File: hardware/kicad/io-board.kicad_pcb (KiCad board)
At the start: 2 copper layers, 160 x 75 mm, 54 parts, among them J1 NCJ6FI-S, J2 NCJ6FI-S, J3 NCJ6FI-S, J4 NCJ6FI-S, P1 JIO-PWR, P2 JIO-WETSEND, P3 JIO-WETRET, P4 JIO-DRY, P5 Wet/Dry control, P6 Mono switch, U1 OPA1644AIDR, U2 OPA1656IDR, U3 OPA1656IDR, U4 OPA1656IDR

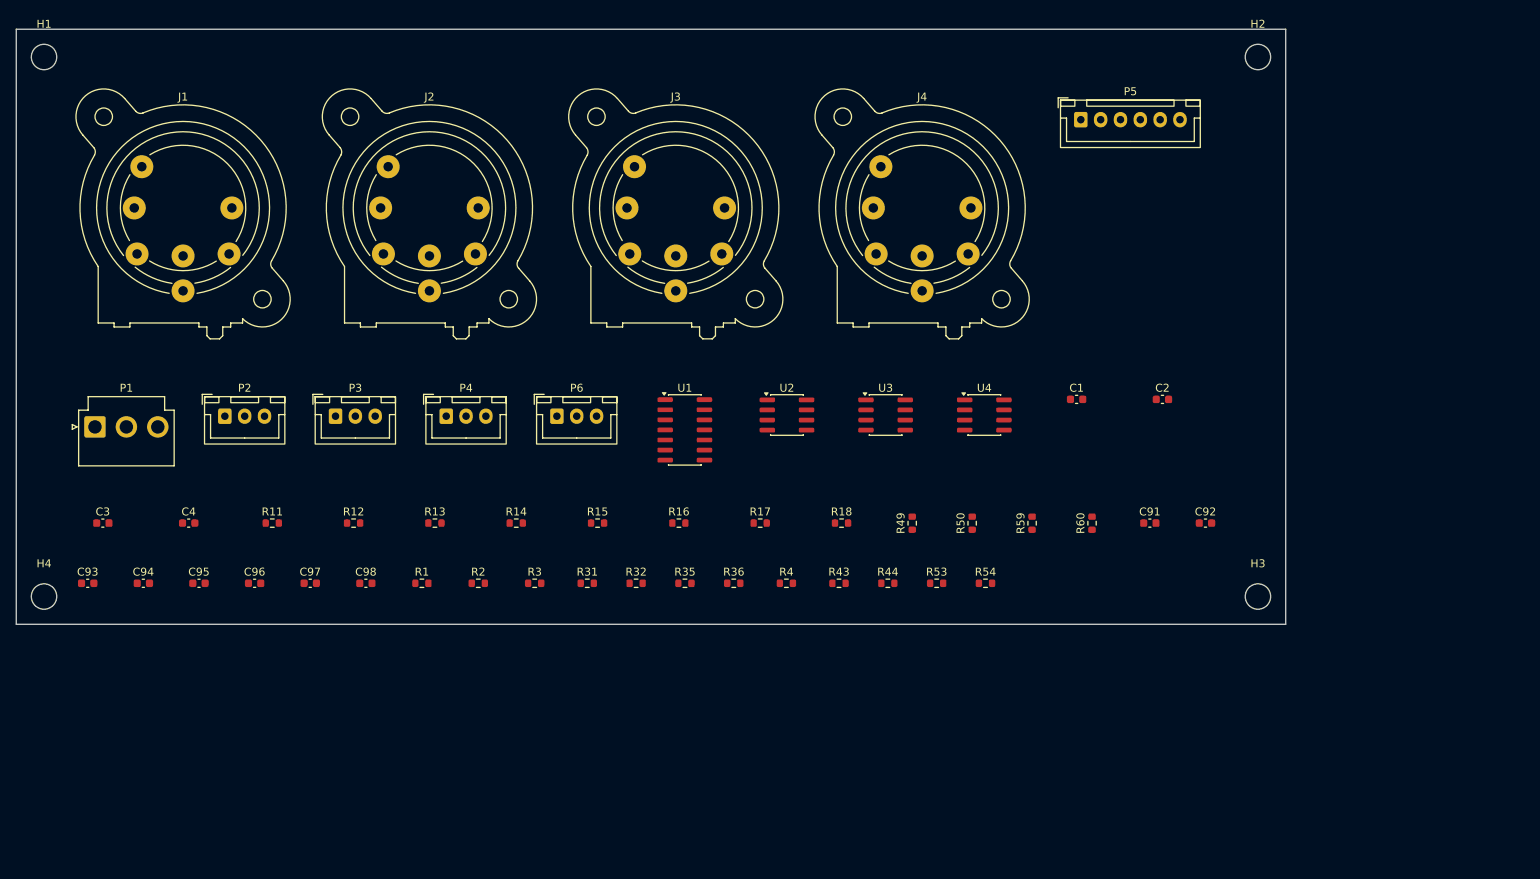
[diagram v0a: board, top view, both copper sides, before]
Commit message: Board 6 io-board complete (ERC 0, sim verified, DRC 0/0 with ground grid stitching); all six boards READY TO ORDER; fab packet with gerber zips, BOMs, pos files, ORDER-PACKET.md; readiness report regenerated
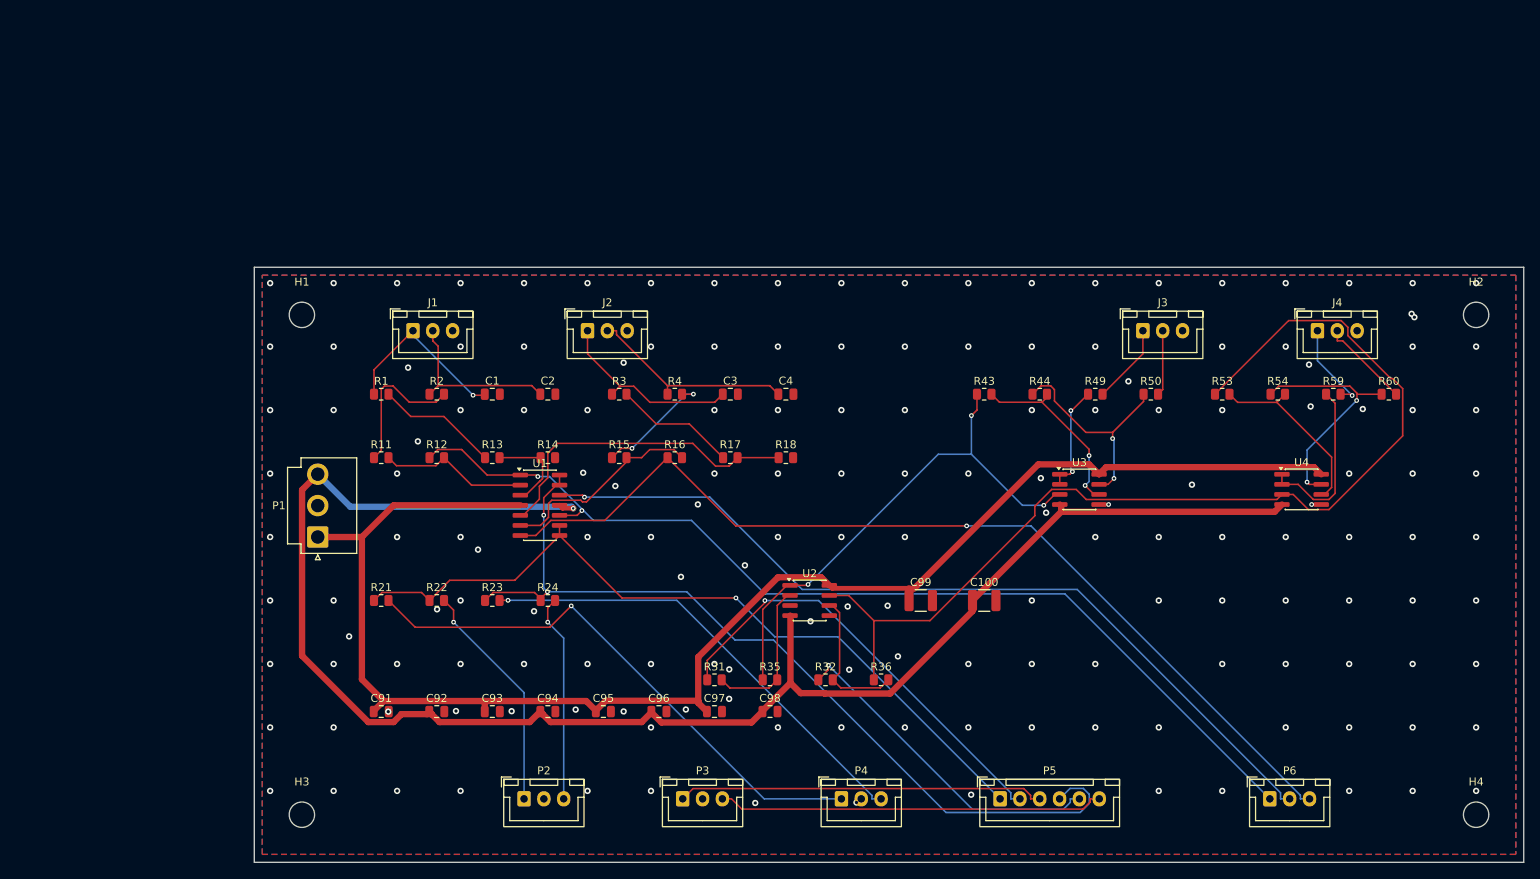
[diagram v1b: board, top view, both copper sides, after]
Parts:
- added C100: 22u, Capacitor_SMD:C_1210_3225Metric, F.Cu at (122.0, 72.0)
- added C99: 22u, Capacitor_SMD:C_1210_3225Metric, F.Cu at (114.0, 72.0)
- added R21: 100, Resistor_SMD:R_0805_2012Metric, F.Cu at (46.0, 72.0)
- added R22: 100, Resistor_SMD:R_0805_2012Metric, F.Cu at (53.0, 72.0)
- added R23: 100, Resistor_SMD:R_0805_2012Metric, F.Cu at (60.0, 72.0)
- added R24: 100, Resistor_SMD:R_0805_2012Metric, F.Cu at (67.0, 72.0)
- C1, C2, C3, C4: value 220p DNP -> 220p; footprint C_0603_1608Metric -> Capacitor_SMD:C_0805_2012Metric
- C91, C92, C93, C94, C95, C96, C97, C98: footprint C_0603_1608Metric -> Capacitor_SMD:C_0805_2012Metric
- H1, H2, H3, H4: value M3 NPTH -> M3; footprint MountingHole_3.2mm_M3 -> MountingHole:MountingHole_3.2mm_M3
- J1: value NCJ6FI-S -> to L IN combo jack; footprint Jack_XLR-6.35mm_Neutrik_NCJ6FI-V_Vertical -> Connector_JST:JST_XH_B3B-XH-A_1x03_P2.50mm_Vertical
- J2: value NCJ6FI-S -> to R IN combo jack; footprint Jack_XLR-6.35mm_Neutrik_NCJ6FI-V_Vertical -> Connector_JST:JST_XH_B3B-XH-A_1x03_P2.50mm_Vertical
- J3: value NCJ6FI-S -> to L OUT combo jack; footprint Jack_XLR-6.35mm_Neutrik_NCJ6FI-V_Vertical -> Connector_JST:JST_XH_B3B-XH-A_1x03_P2.50mm_Vertical
- J4: value NCJ6FI-S -> to R OUT combo jack; footprint Jack_XLR-6.35mm_Neutrik_NCJ6FI-V_Vertical -> Connector_JST:JST_XH_B3B-XH-A_1x03_P2.50mm_Vertical
- P1: value JIO-PWR -> JIO-PWR B3P-VH-B; footprint JST_VH_B3P-VH_1x03_P3.96mm_Vertical -> Connector_JST:JST_VH_B3P-VH_1x03_P3.96mm_Vertical
- P2: value JIO-WETSEND -> P2; footprint JST_XH_B3B-XH-A_1x03_P2.50mm_Vertical -> Connector_JST:JST_XH_B3B-XH-A_1x03_P2.50mm_Vertical
- P3: value JIO-WETRET -> P3; footprint JST_XH_B3B-XH-A_1x03_P2.50mm_Vertical -> Connector_JST:JST_XH_B3B-XH-A_1x03_P2.50mm_Vertical
- P4: value JIO-DRY -> P4; footprint JST_XH_B3B-XH-A_1x03_P2.50mm_Vertical -> Connector_JST:JST_XH_B3B-XH-A_1x03_P2.50mm_Vertical
- P5: value Wet/Dry control -> P5; footprint JST_XH_B6B-XH-A_1x06_P2.50mm_Vertical -> Connector_JST:JST_XH_B6B-XH-A_1x06_P2.50mm_Vertical
- P6: value Mono switch -> P6; footprint JST_XH_B3B-XH-A_1x03_P2.50mm_Vertical -> Connector_JST:JST_XH_B3B-XH-A_1x03_P2.50mm_Vertical
- R1, R2, R3, R4: value 100R -> 100; footprint R_0603_1608Metric -> Resistor_SMD:R_0805_2012Metric
- R11, R12, R13, R14, R15, R16, R17, R18: value 10k 0.1% -> 10k; footprint R_0603_1608Metric -> Resistor_SMD:R_0805_2012Metric
- R31, R32, R35, R36, R43, R44, R53, R54: footprint R_0603_1608Metric -> Resistor_SMD:R_0805_2012Metric
- R49, R50, R59, R60: value 49.9R -> 49.9; footprint R_0603_1608Metric -> Resistor_SMD:R_0805_2012Metric
- U1: footprint SOIC-14_3.9x8.7mm_P1.27mm -> Package_SO:SOIC-14_3.9x8.7mm_P1.27mm
- U2, U3, U4: footprint SOIC-8_3.9x4.9mm_P1.27mm -> Package_SO:SOIC-8_3.9x4.9mm_P1.27mm
- moved H4 182.6 mm to (184.0, 99.0)
- moved H3 123.6 mm to (36.0, 99.0)
- moved P6 102.0 mm to (158.0, 97.0)
- moved C92 99.8 mm to (53.0, 86.0)
- moved C91 99.7 mm to (46.0, 86.0)
- moved P5 86.2 mm to (124.0, 97.0)
- moved C3 80.7 mm to (90.0, 46.0)
- moved C2 77.5 mm to (67.0, 46.0)
- moved C4 77.0 mm to (97.0, 46.0)
- moved C1 73.6 mm to (60.0, 46.0)
- moved P4 69.3 mm to (104.0, 97.0)
- moved P3 65.1 mm to (84.0, 97.0)
- moved P2 61.2 mm to (64.0, 97.0)
- moved J3 54.9 mm to (142.0, 38.0)
- moved C93 53.5 mm to (60.0, 86.0)
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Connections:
- C1 pad 1: (no net) -> IN_BAL_L_P
- C1 pad 2: (no net) -> AGND
- C2 pad 1: (no net) -> IN_BAL_L_N
- C2 pad 2: (no net) -> AGND
- C3 pad 1: (no net) -> IN_BAL_R_P
- C3 pad 2: (no net) -> AGND
- C4 pad 1: (no net) -> IN_BAL_R_N
- C4 pad 2: (no net) -> AGND
- C91 pad 1: (no net) -> +15VA
- C91 pad 2: (no net) -> AGND
- C92 pad 1: (no net) -> -15VA
- C92 pad 2: (no net) -> AGND
- C93 pad 1: (no net) -> +15VA
- C93 pad 2: (no net) -> AGND
- C94 pad 1: (no net) -> -15VA
- C94 pad 2: (no net) -> AGND
- C95 pad 1: (no net) -> +15VA
- C95 pad 2: (no net) -> AGND
- C96 pad 1: (no net) -> -15VA
- C96 pad 2: (no net) -> AGND
- C97 pad 1: (no net) -> +15VA
- C97 pad 2: (no net) -> AGND
- C98 pad 1: (no net) -> -15VA
- C98 pad 2: (no net) -> AGND
- J1 pad 1: (no net) -> IN_BAL_L_P
- J1 pad 2: (no net) -> IN_BAL_L_N
- J1 pad 3: (no net) -> AGND
- J2 pad 1: (no net) -> IN_BAL_R_P
- J2 pad 2: (no net) -> IN_BAL_R_N
- J2 pad 3: (no net) -> AGND
- J3 pad 1: (no net) -> OUT_BAL_L_P
- J3 pad 2: (no net) -> OUT_BAL_L_N
- J3 pad 3: (no net) -> AGND
- J4 pad 1: (no net) -> OUT_BAL_R_P
- J4 pad 2: (no net) -> OUT_BAL_R_N
- J4 pad 3: (no net) -> AGND
- P1 pad 1: (no net) -> +15VA
- P1 pad 2: (no net) -> AGND
- P1 pad 3: (no net) -> -15VA
- P2 pad 1: (no net) -> WET_SEND_L
- P2 pad 2: (no net) -> AGND
- P2 pad 3: (no net) -> WET_SEND_R
- P3 pad 1: (no net) -> WET_SUM_L
- P3 pad 2: (no net) -> AGND
- P3 pad 3: (no net) -> WET_SUM_R
- P4 pad 1: (no net) -> DRY_L
- P4 pad 2: (no net) -> AGND
- P4 pad 3: (no net) -> DRY_R
- P5 pad 1: (no net) -> L_PROG
- P5 pad 2: (no net) -> WD_L_WIPER
- P5 pad 3: (no net) -> WET_SUM_L
- P5 pad 4: (no net) -> R_PROG
- P5 pad 5: (no net) -> WD_R_WIPER
- P5 pad 6: (no net) -> WET_SUM_R
- P6 pad 1: (no net) -> L_RX
- P6 pad 2: (no net) -> MONO_C
- P6 pad 3: (no net) -> R_RX
- R1 pad 1: (no net) -> IN_BAL_L_P
- R1 pad 2: (no net) -> N_INL_P
- R11 pad 1: (no net) -> N_INL_N
- R11 pad 2: (no net) -> N_U1A_M
- R12 pad 1: (no net) -> L_RX
- R12 pad 2: (no net) -> N_U1A_M
- R13 pad 1: (no net) -> N_INL_P
- R13 pad 2: (no net) -> N_U1A_P
- R14 pad 1: (no net) -> N_U1A_P
- R14 pad 2: (no net) -> AGND
- R15 pad 1: (no net) -> N_INR_N
- R15 pad 2: (no net) -> N_U1B_M
- R16 pad 1: (no net) -> R_RX
- R16 pad 2: (no net) -> N_U1B_M
- R17 pad 1: (no net) -> N_INR_P
- R17 pad 2: (no net) -> N_U1B_P
- R18 pad 1: (no net) -> N_U1B_P
- R18 pad 2: (no net) -> AGND
- R2 pad 1: (no net) -> IN_BAL_L_N
- R2 pad 2: (no net) -> N_INL_N
- R3 pad 1: (no net) -> IN_BAL_R_P
- R3 pad 2: (no net) -> N_INR_P
- R31 pad 1: (no net) -> WD_L_WIPER
- R31 pad 2: (no net) -> N_U2A_M
- R32 pad 1: (no net) -> WD_R_WIPER
- R32 pad 2: (no net) -> N_U2B_M
- R35 pad 1: (no net) -> L_BLEND
- R35 pad 2: (no net) -> N_U2A_M
- R36 pad 1: (no net) -> R_BLEND
- R36 pad 2: (no net) -> N_U2B_M
- R4 pad 1: (no net) -> IN_BAL_R_N
- R4 pad 2: (no net) -> N_INR_N
- R43 pad 1: (no net) -> L_BLEND
- R43 pad 2: (no net) -> N_U3B_M
- R44 pad 1: (no net) -> N_COLD_L
- R44 pad 2: (no net) -> N_U3B_M
- R49 pad 1: (no net) -> N_HOT_L
- R49 pad 2: (no net) -> OUT_BAL_L_P
- R50 pad 1: (no net) -> N_COLD_L
- R50 pad 2: (no net) -> OUT_BAL_L_N
- R53 pad 1: (no net) -> R_BLEND
- R53 pad 2: (no net) -> N_U4B_M
- R54 pad 1: (no net) -> N_COLD_R
- R54 pad 2: (no net) -> N_U4B_M
- R59 pad 1: (no net) -> N_HOT_R
- R59 pad 2: (no net) -> OUT_BAL_R_P
- R60 pad 1: (no net) -> N_COLD_R
- R60 pad 2: (no net) -> OUT_BAL_R_N
- U1 pad 1: (no net) -> L_RX
- U1 pad 10: (no net) -> L_RX
- U1 pad 11: (no net) -> -15VA
- U1 pad 12: (no net) -> MONO_C
- U1 pad 13: (no net) -> R_PROG
- U1 pad 14: (no net) -> R_PROG
- U1 pad 2: (no net) -> N_U1A_M
- U1 pad 3: (no net) -> N_U1A_P
- U1 pad 4: (no net) -> +15VA
- U1 pad 5: (no net) -> N_U1B_P
- U1 pad 6: (no net) -> N_U1B_M
- U1 pad 7: (no net) -> R_RX
- U1 pad 8: (no net) -> L_PROG
- U1 pad 9: (no net) -> L_PROG
- U2 pad 1: (no net) -> L_BLEND
- U2 pad 2: (no net) -> N_U2A_M
- U2 pad 3: (no net) -> AGND
- U2 pad 4: (no net) -> -15VA
- U2 pad 5: (no net) -> AGND
- U2 pad 6: (no net) -> N_U2B_M
- U2 pad 7: (no net) -> R_BLEND
- U2 pad 8: (no net) -> +15VA
- U3 pad 1: (no net) -> N_HOT_L
- U3 pad 2: (no net) -> N_HOT_L
- U3 pad 3: (no net) -> L_BLEND
- U3 pad 4: (no net) -> -15VA
- U3 pad 5: (no net) -> AGND
- U3 pad 6: (no net) -> N_U3B_M
- U3 pad 7: (no net) -> N_COLD_L
- U3 pad 8: (no net) -> +15VA
- U4 pad 1: (no net) -> N_HOT_R
- U4 pad 2: (no net) -> N_HOT_R
- U4 pad 3: (no net) -> R_BLEND
- U4 pad 4: (no net) -> -15VA
- U4 pad 5: (no net) -> AGND
- U4 pad 6: (no net) -> N_U4B_M
- U4 pad 7: (no net) -> N_COLD_R
- U4 pad 8: (no net) -> +15VA
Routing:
- net -15VA: track 0.00 -> 212.8 mm, vias 0 -> 1
- net +15VA: track 0.00 -> 192.8 mm
- net R_BLEND: track 0.00 -> 131.6 mm
- net L_RX: track 0.00 -> 127.8 mm, vias 0 -> 2
- net R_RX: track 0.00 -> 121.6 mm, vias 0 -> 1
- net R_PROG: track 0.00 -> 111.2 mm, vias 0 -> 2
- net MONO_C: track 0.00 -> 108.3 mm, vias 0 -> 1
- net L_PROG: track 0.00 -> 98.2 mm, vias 0 -> 1
- net DRY_L: track 0.00 -> 69.7 mm, vias 0 -> 1
- net L_BLEND: track 0.00 -> 65.5 mm, vias 0 -> 3
- net DRY_R: track 0.00 -> 58.7 mm, vias 0 -> 1
- net WD_L_WIPER: track 0.00 -> 55.9 mm, vias 0 -> 1
- net WET_SUM_R: track 0.00 -> 48.8 mm
- net WET_SUM_L: track 0.00 -> 46.3 mm
- net WD_R_WIPER: track 0.00 -> 42.3 mm, vias 0 -> 1
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- added copper zone on B.Cu, net AGND
- added copper zone on F.Cu, net AGND
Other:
- board text removed: "GAS Rev A - Input / Output Board"
- board text removed: "OUTLINE SCAFFOLD - NOT FOR FAB"

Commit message: Schematic review (kicad-schematic-review skill): F1 R-78E moved to +15VRAW, F2 mono-float bleed R25; both boards re-routed/verified; datasheet cache, per-instance reviews, schematic_review.md
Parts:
- added U1: OPA1644AIDR, Package_SO:SOIC-14_3.9x8.7mm_P1.27mm, F.Cu at (66.0, 60.0)
- R25: renamed from R3; value 100 -> 1Meg
- R3: renamed from R31; value 20k -> 100
- R36: renamed from R4; value 100 -> 20k
- R4: renamed from R43; value 10k -> 100
- R44: renamed from R49; value 49.9 -> 10k
- R50: renamed from R53; value 10k -> 49.9
- R54: renamed from R59; value 49.9 -> 10k
- R60: renamed from U1; value OPA1644AIDR -> 49.9; footprint Package_SO:SOIC-14_3.9x8.7mm_P1.27mm -> Resistor_SMD:R_0805_2012Metric
- moved R60 107.9 mm to (173.0, 46.0)
- moved R25 83.4 mm to (148.0, 88.0)
- moved R36 44.4 mm to (109.0, 82.0)
- moved R4 39.0 mm to (83.0, 46.0)
- moved R3 37.9 mm to (76.0, 46.0)
- moved R31 14.0 mm to (88.0, 82.0)
- moved R35 14.0 mm to (95.0, 82.0)
- moved R50 9.00 mm to (143.0, 46.0)
- moved R32 7.00 mm to (102.0, 82.0)
- moved R43 7.00 mm to (122.0, 46.0)
- moved R44 7.00 mm to (129.0, 46.0)
- moved R49 7.00 mm to (136.0, 46.0)
- moved R53 7.00 mm to (152.0, 46.0)
- moved R54 7.00 mm to (159.0, 46.0)
- moved R59 7.00 mm to (166.0, 46.0)
- renumbered R32 to R31, R35 to R32, R36 to R35, R44 to R43, R50 to R49, R54 to R53, R60 to R59
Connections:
- R25 pad 1: IN_BAL_R_P -> MONO_C
- R25 pad 2: N_INR_P -> R_RX
- R3 pad 1: WD_L_WIPER -> IN_BAL_R_P
- R3 pad 2: N_U2A_M -> N_INR_P
- R31 pad 1: WD_R_WIPER -> WD_L_WIPER
- R31 pad 2: N_U2B_M -> N_U2A_M
- R32 pad 1: L_BLEND -> WD_R_WIPER
- R32 pad 2: N_U2A_M -> N_U2B_M
- R35 pad 1: R_BLEND -> L_BLEND
- R35 pad 2: N_U2B_M -> N_U2A_M
- R36 pad 1: IN_BAL_R_N -> R_BLEND
- R36 pad 2: N_INR_N -> N_U2B_M
- R4 pad 1: L_BLEND -> IN_BAL_R_N
- R4 pad 2: N_U3B_M -> N_INR_N
- R43 pad 1: N_COLD_L -> L_BLEND
- R44 pad 1: N_HOT_L -> N_COLD_L
- R44 pad 2: OUT_BAL_L_P -> N_U3B_M
- R49 pad 1: N_COLD_L -> N_HOT_L
- R49 pad 2: OUT_BAL_L_N -> OUT_BAL_L_P
- R50 pad 1: R_BLEND -> N_COLD_L
- R50 pad 2: N_U4B_M -> OUT_BAL_L_N
- R53 pad 1: N_COLD_R -> R_BLEND
- R54 pad 1: N_HOT_R -> N_COLD_R
- R54 pad 2: OUT_BAL_R_P -> N_U4B_M
- R59 pad 1: N_COLD_R -> N_HOT_R
- R59 pad 2: OUT_BAL_R_N -> OUT_BAL_R_P
- R60 pad 1: L_RX -> N_COLD_R
- R60 pad 2: N_U1A_M -> OUT_BAL_R_N
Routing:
- net N_HOT_R: track 22.0 -> 53.9 mm
- net L_BLEND: track 65.5 -> 96.8 mm, vias 3 -> 0
- net -15VA: track 212.8 -> 186.9 mm, vias 1 -> 2
- net R_RX: track 121.6 -> 139.7 mm
- net WD_L_WIPER: track 55.9 -> 46.1 mm, vias 1 -> 0
- net R_PROG: track 111.2 -> 102.6 mm
- net +15VA: track 192.8 -> 189.8 mm, vias 0 -> 2
- net WD_R_WIPER: track 42.3 -> 39.4 mm, vias 1 -> 0
- net L_RX: track 127.8 -> 130.4 mm
- net N_COLD_R: track 30.5 -> 33.0 mm, vias 2 -> 0
- net N_U2A_M: track 19.4 -> 21.7 mm, vias 0 -> 2
- net OUT_BAL_R_P: track 11.5 -> 9.21 mm, vias 1 -> 0
- net DRY_L: track 69.7 -> 67.4 mm
- net R_BLEND: track 131.6 -> 133.7 mm, vias 0 -> 2
- net L_PROG: track 98.2 -> 99.3 mm
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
